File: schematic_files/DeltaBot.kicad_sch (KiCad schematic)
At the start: 15 parts, among them J1 USB C PD Modulle, J3 MOTOR_L, J4 MOTOR_R, J5 C1_LIDAR, SW1 SW_SPDT, U1 Radxa_ROCK5B, U2 Buck Converter

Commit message: file org changes and camera.cpp draft
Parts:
- C1: footprint deltabot:CP_Radial_D12.5mm_P5.00mm -> Capacitor_THT:CP_Radial_D12.5mm_P5.00mm
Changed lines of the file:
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@@
 			)
 		)
-		(property "Footprint" "deltabot:CP_Radial_D12.5mm_P5.00mm"
+		(property "Footprint" "Capacitor_THT:CP_Radial_D12.5mm_P5.00mm"
 			(at 54.3052 71.12 0)
 			(effects

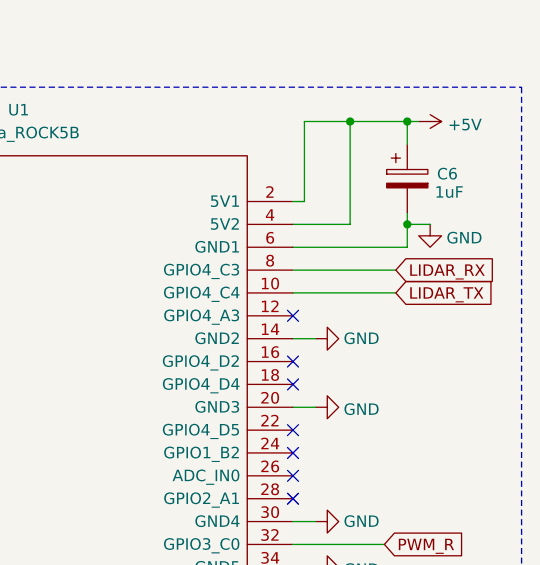
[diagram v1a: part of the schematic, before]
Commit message: drill holes added for battery pack platform and edgecuts for ports
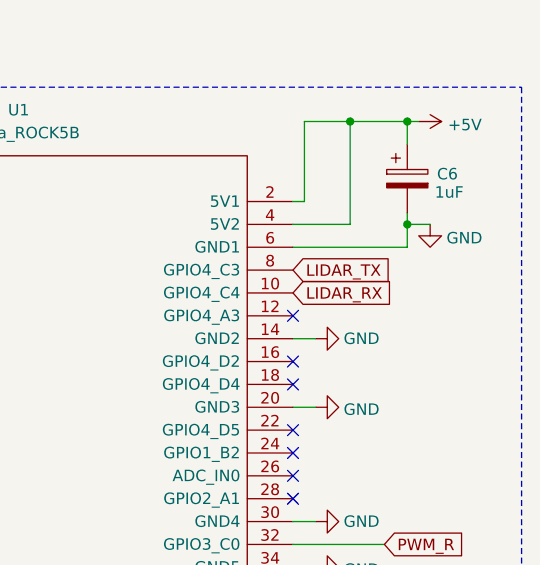
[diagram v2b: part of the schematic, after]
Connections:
- net LIDAR_RX: now also U1.10 (GPIO4_C4); no longer U1.8 (GPIO4_C3)
- net LIDAR_TX: now also U1.8 (GPIO4_C3); no longer U1.10 (GPIO4_C4)
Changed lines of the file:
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@@
-	(wire
-		(pts
-			(xy 168.91 41.91) (xy 180.34 41.91)
-		)
-		(stroke
-			(width 0)
-			(type default)
-		)
-	)
 	(wire
 		(pts
@@
 		(pts
 			(xy 33.02 115.57) (xy 34.29 115.57)
-		)
-		(stroke
-			(width 0)
-			(type default)
-		)
-	)
-	(wire
-		(pts
-			(xy 168.91 44.45) (xy 180.34 44.45)
 		)
 		(stroke
@@
 	(global_label "LIDAR_RX"
 		(shape input)
-		(at 180.34 41.91 0)
+		(at 168.91 44.45 0)
 		(effects
 			(font
@@
 		)
 		(property "Intersheetrefs" "${INTERSHEET_REFS}"
-			(at 180.34 41.91 0)
+			(at 168.91 44.45 0)
 			(effects
 				(font
@@
 	(global_label "LIDAR_TX"
 		(shape input)
-		(at 180.34 44.45 0)
+		(at 168.91 41.91 0)
 		(effects
 			(font
@@
 		)
 		(property "Intersheetrefs" "${INTERSHEET_REFS}"
-			(at 180.34 44.45 0)
+			(at 168.91 41.91 0)
 			(effects
 				(font
